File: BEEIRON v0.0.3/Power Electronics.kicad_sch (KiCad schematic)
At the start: 14 parts, among them J12 Conn_01x02_Male, Q1 BTB26-600, U7 MOC3020M, U8 4N25

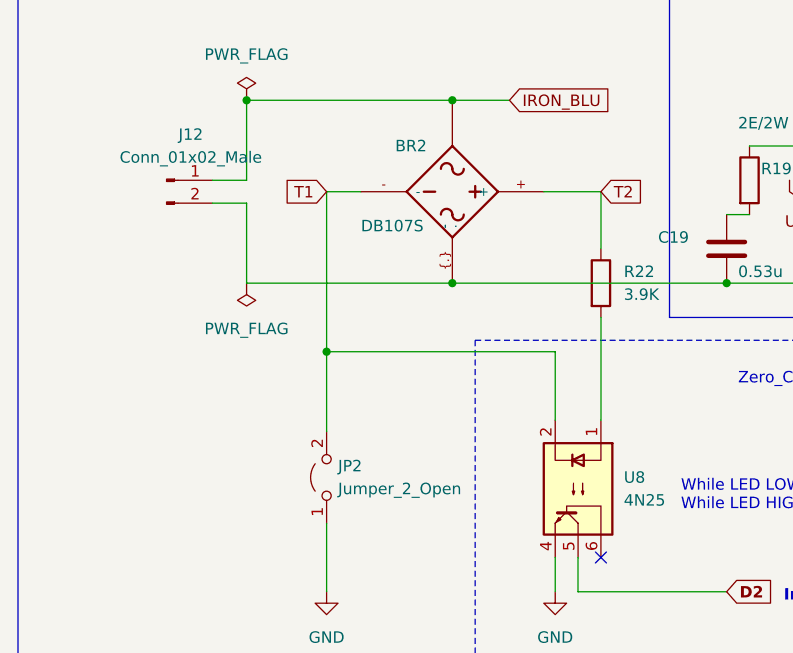
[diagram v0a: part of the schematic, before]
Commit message: minor edit in the schematics
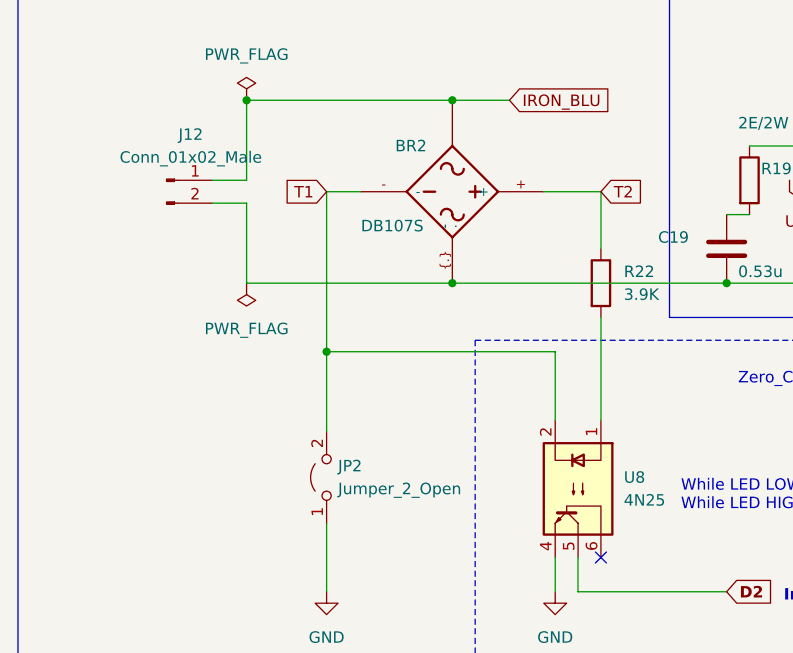
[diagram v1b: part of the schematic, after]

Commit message: added bakup file
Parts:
- renumbered JP2 to JP8, Q1 to Q7, R17 to R26, R18 to R27, R19 to R28, R20 to R29, R21 to R30, R22 to R31
